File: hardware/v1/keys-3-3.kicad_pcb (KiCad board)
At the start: 2 copper layers, 12.7 x 101.6 mm, 10 parts, among them P35 CONN_01X04, P36 CONN_01X08, P37 CONN_01X08, SW27 SWITCH_INV, SW28 SWITCH_INV, SW29 SWITCH_INV, U9 MCP23017

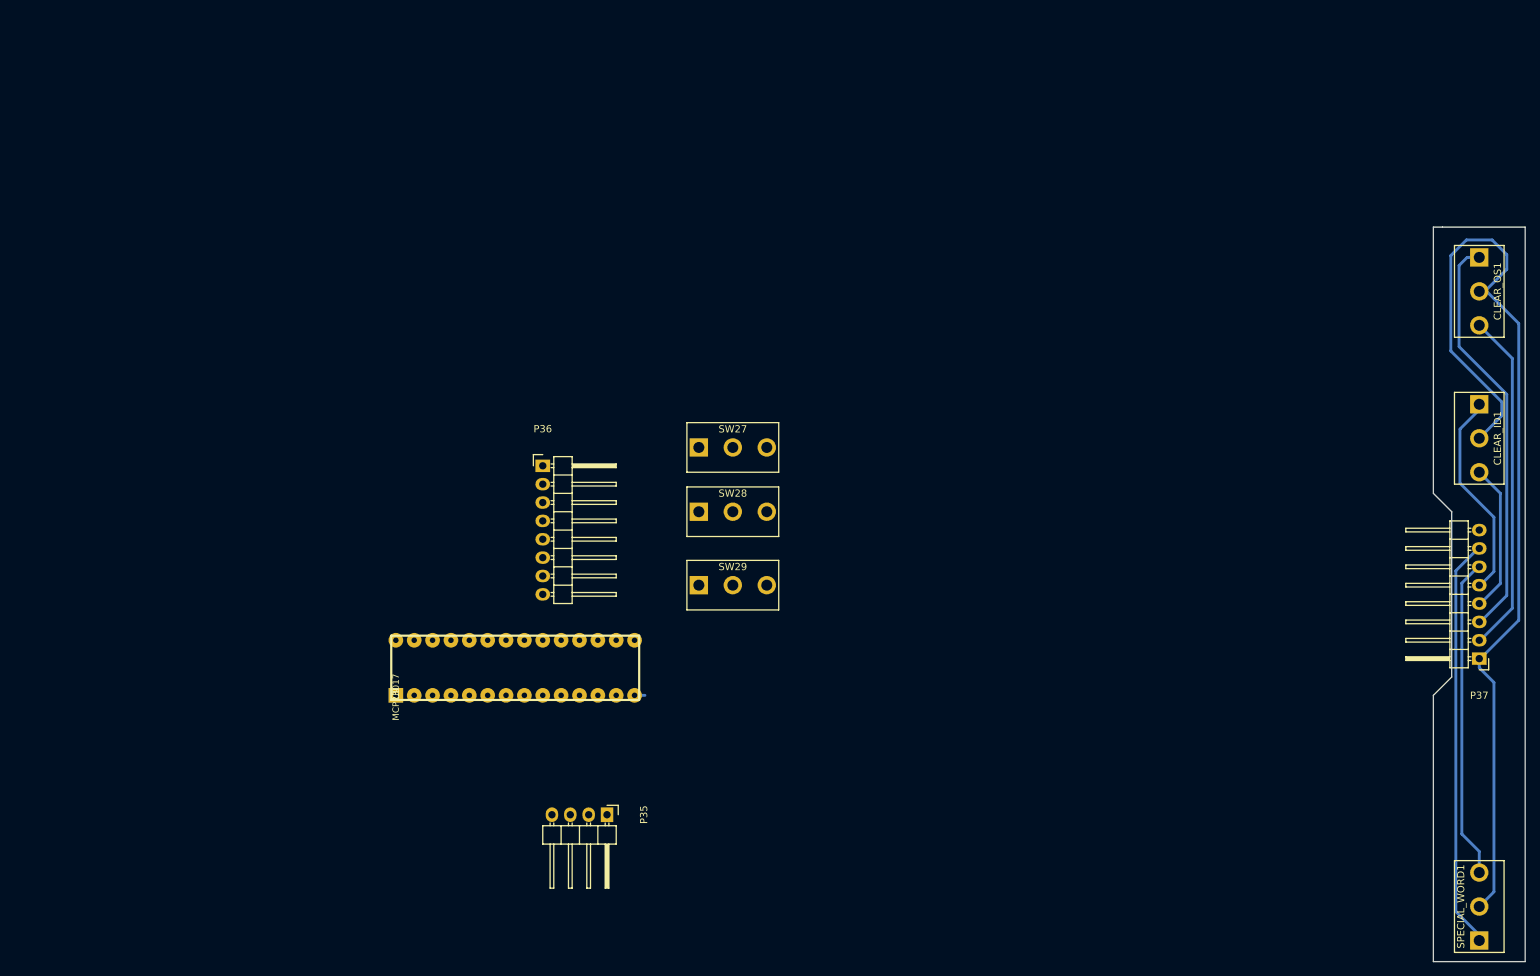
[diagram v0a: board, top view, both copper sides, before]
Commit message: Integrate first set of switches
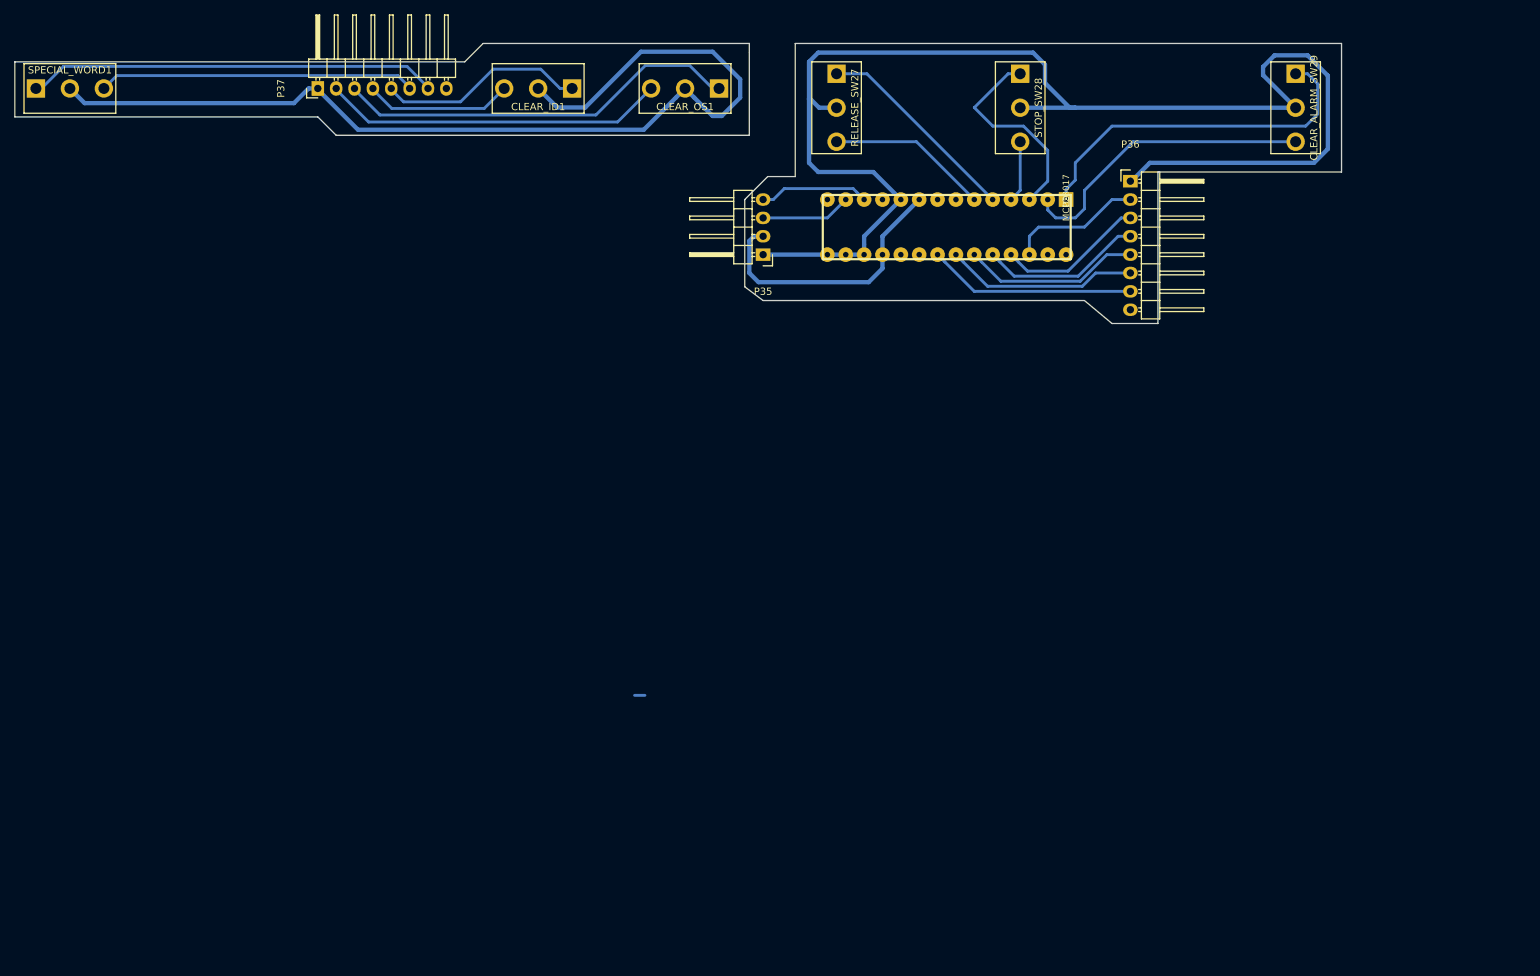
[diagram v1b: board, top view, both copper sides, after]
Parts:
- moved SPECIAL_WORD1 225.4 mm to (46.4, 35.4), turned to 0 degrees
- moved P37 179.0 mm to (80.6, 35.4), turned to 90 degrees
- moved CLEAR_ID1 138.9 mm to (111.1, 35.4), turned to 180 degrees
- moved U9 115.3 mm to (184.2, 50.8), turned to 180 degrees
- moved CLEAR_OS1 113.4 mm to (131.4, 35.4), turned to 180 degrees
- moved CLEAR_ALARM_SW29 102.1 mm to (215.9, 38.1), turned to 270 degrees
- moved P36 90.3 mm to (193.0, 48.3)
- moved P35 80.4 mm to (142.2, 58.4), turned to 180 degrees
- moved STOP_SW28 68.6 mm to (177.8, 38.1), turned to 270 degrees
- moved RELEASE_SW27 49.1 mm to (152.4, 38.1), turned to 270 degrees
- renumbered SW29 to CLEAR_ALARM_SW29, SW27 to RELEASE_SW27, SW28 to STOP_SW28
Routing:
- net GND: track 0.00 -> 194.6 mm
- net Net-(CLEAR_ALARM_SW29-Pad1): track 0.00 -> 49.7 mm
- net Net-(CLEAR_ALARM_SW29-Pad3): track 0.00 -> 42.0 mm
- net VDD: track 0.00 -> 38.0 mm
- net Net-(RELEASE_SW27-Pad1): track 0.00 -> 28.8 mm
- net /SPECIAL_A: track 0.00 -> 28.8 mm
- net Net-(STOP_SW28-Pad1): track 0.00 -> 28.8 mm
- net /SPECIAL_B: track 0.00 -> 26.7 mm
- net /CLEAR_ID_A: track 0.00 -> 24.6 mm
- net /CLEAR_ID_B: track 0.00 -> 22.6 mm
- net Net-(RELEASE_SW27-Pad3): track 0.00 -> 22.4 mm
- net /CLEAR_OS_A: track 0.00 -> 20.5 mm
- net /CLEAR_OS_B: track 0.00 -> 18.6 mm
- net /SCK: track 0.00 -> 15.2 mm
- net /SDA: track 0.00 -> 12.5 mm
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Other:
- board size 12.7 x 101.6 mm -> 183.5 x 38.7 mm
